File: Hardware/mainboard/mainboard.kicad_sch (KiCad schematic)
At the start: 31 parts, among them J1 Conn_01x06_Socket, J2 559592430, J3 USB_C_Receptacle_PowerOnly_24P, J5 SBH11-PBPC-D05-ST-BK, SW1 SW_SPDT, SW2 Board reset, SW3 Big reset, U1 S16B-PHDSSLFSN, U2 AMS1117-3.3, U3 STM32F091RCTx, Y1 16MHz

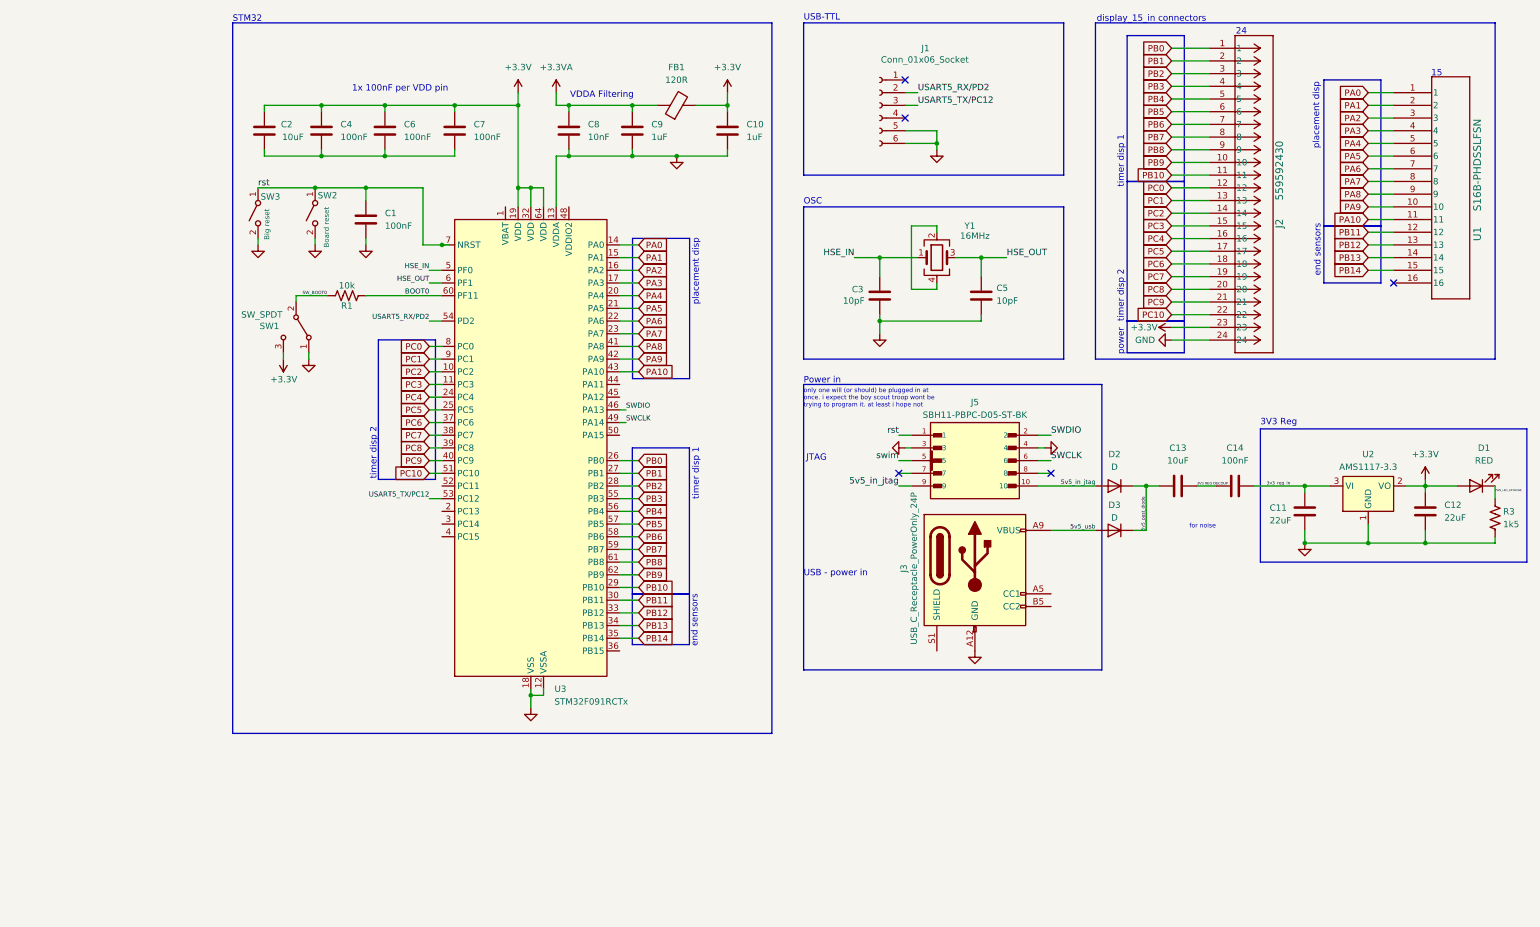
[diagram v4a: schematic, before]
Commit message: updated schematic
added:
-footprints
-status leds
-libraries
-connectors

separated into sheets since too many components on pange
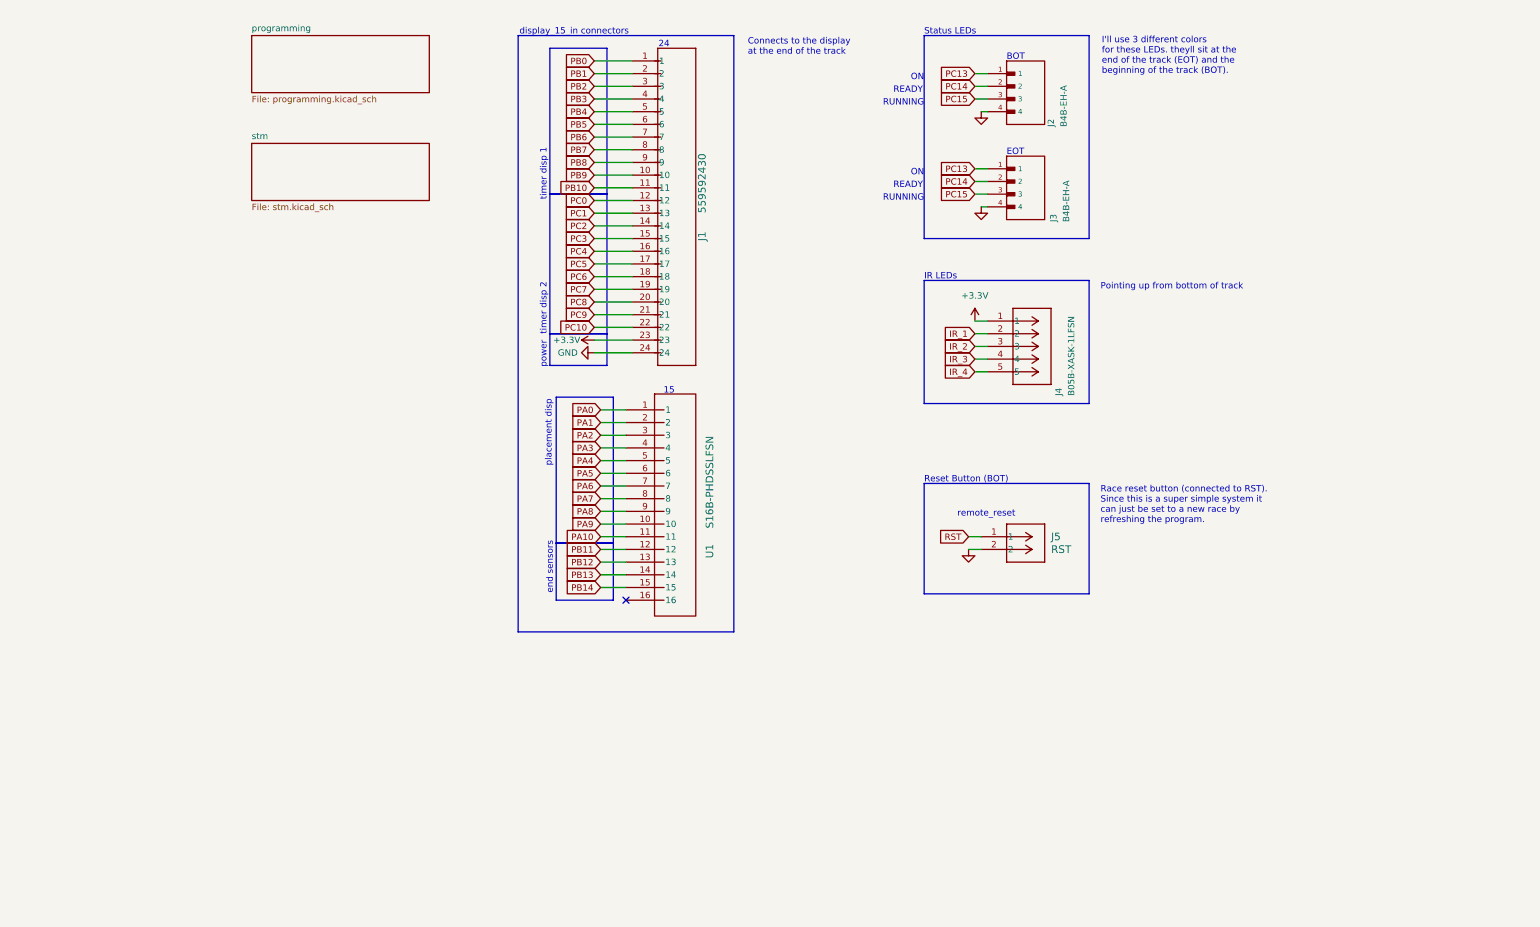
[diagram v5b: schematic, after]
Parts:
- removed C1, C14, C4, C6, C7: 100nF, Capacitor_SMD:C_0805_2012Metric, symbol Device:C
- removed C10, C9: 1uF, Capacitor_SMD:C_0805_2012Metric, symbol Device:C
- removed C11, C12: 22uF, Capacitor_SMD:C_0805_2012Metric, symbol Device:C
- removed C13, C2: 10uF, Capacitor_SMD:C_0805_2012Metric, symbol Device:C
- removed C3, C5: 10pF, Capacitor_SMD:C_0805_2012Metric, symbol Device:C
- removed C8: 10nF, Capacitor_SMD:C_0805_2012Metric, symbol Device:C
- removed D1: RED, Diode_SMD:D_0805_2012Metric, symbol Device:LED
- removed D2, D3: D, symbol Device:D
- removed FB1: 120R, Resistor_SMD:R_0805_2012Metric_Pad1.20x1.40mm_HandSolder, symbol Device:FerriteBead
- removed J1: Conn_01x06_Socket, jtag:SULLINS_SBH11-PBPC-D05-ST-BK, symbol Connector:Conn_01x06_Socket
- removed J3: USB_C_Receptacle_PowerOnly_24P, symbol Connector:USB_C_Receptacle_PowerOnly_24P
- removed J5: SBH11-PBPC-D05-ST-BK, SBH11-PBPC-D05-ST-BK:SULLINS_SBH11-PBPC-D05-ST-BK, symbol jtag:SBH11-PBPC-D05-ST-BK
- removed R1: 10k, Resistor_SMD:R_0805_2012Metric_Pad1.20x1.40mm_HandSolder, symbol Device:R_US
- removed R3: 1k5, Resistor_SMD:R_0805_2012Metric_Pad1.20x1.40mm_HandSolder, symbol Device:R_US
- removed SW1: SW_SPDT, symbol Switch:SW_SPDT
- removed SW2: Board reset, symbol Switch:SW_SPST
- removed SW3: Big reset, symbol Switch:SW_SPST
- removed U2: AMS1117-3.3, 3v3reg:SOT23-BEC, symbol Regulator_Linear:AMS1117-3.3
- removed U3: STM32F091RCTx, Package_QFP:LQFP-64_10x10mm_P0.5mm, symbol MCU_ST_STM32F0:STM32F091RCTx
- removed Y1: 16MHz, crystal smd:OSC_ECS-2520S25-250-FN-TR, symbol Device:Crystal_GND24
- added J2, J3: B4B-EH-A, 1x04_jst_connector:1x04_jst, symbol 1x04_jst:B4B-EH-A
- added J4: B05B-XASK-1LFSN, 1X05_JST:1x05_jst, symbol 1x05_jst:B05B-XASK-1LFSN
- added J5: RST, 1x02_jst_conn:CONN_B02B-XASK-1LFSN_JST, symbol 1x02_jst:B02B-XASK-1LFSN
- J1: renamed from J2; footprint 24pos 2mm:CONN24_559592430_MOL -> CONN24_559592430_MOL
- U1: footprint 16pos 2mm:S16B-PHDSSLFSN_JST -> S16B-PHDSSLFSN_JST
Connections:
- net +3.3V: now also J4.1
- net GND: now also J2.4, J3.4, J5.2
- new net IR_1: J4.2
- new net IR_2: J4.3
- new net IR_3: J4.4
- new net IR_4: J4.5
- new net PC13: J2.1, J3.1
- new net PC14: J2.2, J3.2
- new net PC15: J2.3, J3.3
- new net RST: J5.1
- no-connect marks 5 -> 1
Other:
- added sheet programming (programming.kicad_sch)
- added sheet stm (stm.kicad_sch)
- note added: "BOT"
- note added: "Connects to the display at the end of the track"
- note added: "EOT"
- note added: "I'll use 3 different colors for these LEDs. theyll sit at the end of the track (EOT) and the beginning of the track (BOT)."
- note added: "IR LEDs"
- note added: "ON"
- note added: "Pointing up from bottom of track"
- note added: "READY"
- note added: "RUNNING"
- note added: "Race reset button (connected to RST). Since this is a super simple system it can just be set to a new race by refreshing the program."
- note added: "Reset Button (BOT)"
- note added: "Status LEDs"
- note added: "remote_reset"
- note removed: "1x 100nF per VDD pin"
- note removed: "3V3 Reg"
- note removed: "JTAG"
- note removed: "OSC"
- note removed: "Power in"
- note removed: "STM32"
- note removed: "USB - power in"
- note removed: "USB-TTL"
- note removed: "VDDA Filtering"
- note removed: "for noise"
- note removed: "only one will (or should) be plugged in at once. i expect the boy scout troop wont be trying to program it. at least i hope not"

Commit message: pushing for the evening
didnt add much, just moved things around and fixed footprints
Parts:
- removed J5: RST, 1x02_jst_conn:CONN_B02B-XASK-1LFSN_JST, symbol 1x02_jst:B02B-XASK-1LFSN
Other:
- note removed: "Race reset button (connected to RST). Since this is a super simple system it can just be set to a new race by refreshing the program."
- note removed: "Reset Button (BOT)"
- note removed: "remote_reset"
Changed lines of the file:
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@@
 	(title_block
 		(title "F091RCT6 mainboard")
+		(date "2025-08-03")
 	)
 	(no_connect
@@
 	(wire
 		(pts
-			(xy 161.29 120.65) (xy 163.83 120.65)
-		)
-		(stroke
-			(width 0)
-			(type default)
-		)
-	)
-	(wire
-		(pts
 			(xy 92.71 95.25) (xy 87.63 95.25)
 		)
@@
 		(pts
 			(xy 86.36 50.8) (xy 93.98 50.8)
-		)
-		(stroke
-			(width 0)
-			(type default)
-		)
-	)
-	(wire
-		(pts
-			(xy 161.29 118.11) (xy 163.83 118.11)
 		)
 		(stroke
@@
 	)
 	(rectangle
-		(start 152.4 107.442)
-		(end 185.42 129.54)
-		(stroke
-			(width 0)
-			(type default)
-		)
-		(fill
-			(type none)
-		)
-	)
-	(rectangle
 		(start 77.47 49.53)
 		(end 88.9 77.47)
@@
 		)
 	)
-	(text "Reset Button (BOT)\n"
-		(exclude_from_sim no)
-		(at 152.4 106.68 0)
+	(text "BOT"
+		(exclude_from_sim no)
+		(at 168.91 22.098 0)
 		(effects
 			(font
@@
 		)
 	)
-	(text "remote_reset\n"
-		(exclude_from_sim no)
-		(at 164.846 113.538 0)
-		(effects
-			(font
-				(size 1.27 1.27)
-			)
-		)
-	)
-	(text "BOT"
-		(exclude_from_sim no)
-		(at 168.91 22.098 0)
+	(text "power\n"
+		(exclude_from_sim no)
+		(at 76.2 84.328 90)
 		(effects
 			(font
@@
 		)
 	)
-	(text "power\n"
-		(exclude_from_sim no)
-		(at 76.2 84.328 90)
+	(text "Connects to the display \nat the end of the track"
+		(exclude_from_sim no)
+		(at 117.094 18.288 0)
+		(effects
+			(font
+				(size 1.27 1.27)
+			)
+			(justify left top)
+		)
+	)
+	(text "I'll use 3 different colors\nfor these LEDs. theyll sit at the\nend of the track (EOT) and the\nbeginning of the track (BOT)."
+		(exclude_from_sim no)
+		(at 187.96 18.034 0)
+		(effects
+			(font
+				(size 1.27 1.27)
+			)
+			(justify left top)
+		)
+	)
+	(text "READY"
+		(exclude_from_sim no)
+		(at 152.146 28.702 0)
+		(effects
+			(font
+				(size 1.27 1.27)
+			)
+			(justify right)
+		)
+	)
+	(text "READY"
+		(exclude_from_sim no)
+		(at 152.146 47.752 0)
+		(effects
+			(font
+				(size 1.27 1.27)
+			)
+			(justify right)
+		)
+	)
+	(text "24\n"
+		(exclude_from_sim no)
+		(at 100.33 19.558 0)
+		(effects
+			(font
+				(size 1.27 1.27)
+			)
+		)
+	)
+	(text "15"
+		(exclude_from_sim no)
+		(at 101.346 88.9 0)
+		(effects
+			(font
+				(size 1.27 1.27)
+			)
+		)
+	)
+	(text "RUNNING\n"
+		(exclude_from_sim no)
+		(at 152.4 50.292 0)
+		(effects
+			(font
+				(size 1.27 1.27)
+			)
+			(justify right)
+		)
+	)
+	(text "timer disp 2\n\n"
+		(exclude_from_sim no)
+		(at 77.216 77.724 90)
 		(effects
 			(font
@@
 		)
 	)
-	(text "Connects to the display \nat the end of the track"
-		(exclude_from_sim no)
-		(at 117.094 18.288 0)
-		(effects
-			(font
-				(size 1.27 1.27)
-			)
-			(justify left top)
-		)
-	)
-	(text "I'll use 3 different colors\nfor these LEDs. theyll sit at the\nend of the track (EOT) and the\nbeginning of the track (BOT)."
-		(exclude_from_sim no)
-		(at 187.96 18.034 0)
-		(effects
-			(font
-				(size 1.27 1.27)
-			)
-			(justify left top)
-		)
-	)
-	(text "READY"
-		(exclude_from_sim no)
-		(at 152.146 28.702 0)
-		(effects
-			(font
-				(size 1.27 1.27)
-			)
-			(justify right)
-		)
-	)
-	(text "READY"
-		(exclude_from_sim no)
-		(at 152.146 47.752 0)
-		(effects
-			(font
-				(size 1.27 1.27)
-			)
-			(justify right)
-		)
-	)
-	(text "24\n"
-		(exclude_from_sim no)
-		(at 100.33 19.558 0)
-		(effects
-			(font
-				(size 1.27 1.27)
-			)
-		)
-	)
-	(text "15"
-		(exclude_from_sim no)
-		(at 101.346 88.9 0)
-		(effects
-			(font
-				(size 1.27 1.27)
-			)
-		)
-	)
-	(text "RUNNING\n"
-		(exclude_from_sim no)
-		(at 152.4 50.292 0)
-		(effects
-			(font
-				(size 1.27 1.27)
-			)
-			(justify right)
-		)
-	)
-	(text "Race reset button (connected to RST).\nSince this is a super simple system it\ncan just be set to a new race by \nrefreshing the program."
-		(exclude_from_sim no)
-		(at 187.706 107.95 0)
-		(effects
-			(font
-				(size 1.27 1.27)
-			)
-			(justify left top)
-		)
-	)
-	(text "timer disp 2\n\n"
-		(exclude_from_sim no)
-		(at 77.216 77.724 90)
+	(text "timer disp 1\n"
+		(exclude_from_sim no)
+		(at 76.2 50.8 90)
 		(effects
 			(font
@@
 		)
 	)
-	(text "timer disp 1\n"
-		(exclude_from_sim no)
-		(at 76.2 50.8 90)
-		(effects
-			(font
-				(size 1.27 1.27)
-			)
-			(justify left)
-		)
-	)
 	(global_label "PB4"
 		(shape input)
@@
 		(property "Intersheetrefs" "${INTERSHEET_REFS}"
 			(at 154.6158 49.53 0)
-			(effects
-				(font
-					(size 1.27 1.27)
-				)
-				(justify right)
-				(hide yes)
-			)
-		)
-	)
-	(global_label "RST"
-		(shape input)
-		(at 161.29 118.11 180)
-		(fields_autoplaced yes)
-		(effects
-			(font
-				(size 1.27 1.27)
-			)
-			(justify right)
-		)
-		(property "Intersheetrefs" "${INTERSHEET_REFS}"
-			(at 154.8577 118.11 0)
 			(effects
 				(font
@@
 	)
 	(symbol
-		(lib_id "power:GND")
-		(at 161.29 120.65 0)
-		(mirror y)
-		(unit 1)
-		(exclude_from_sim no)
-		(in_bom yes)
-		(on_board yes)
-		(dnp no)
-		(property "Reference" "#PWR06"
-			(at 161.29 127 0)
-			(effects
-				(font
-					(size 1.27 1.27)
-				)
-				(hide yes)
-			)
-		)
-		(property "Value" "GND"
-			(at 161.29 125.73 0)
-			(effects
-				(font
-					(size 1.27 1.27)
-				)
-				(hide yes)
-			)
-		)
-		(property "Footprint" ""
-			(at 161.29 120.65 0)
-			(effects
-				(font
-					(size 1.27 1.27)
-				)
-				(hide yes)
-			)
-		)
-		(property "Datasheet" ""
-			(at 161.29 120.65 0)
-			(effects
-				(font
-					(size 1.27 1.27)
-				)
-				(hide yes)
-			)
-		)
-		(property "Description" "Power symbol creates a global label with name \"GND\" , ground"
-			(at 161.29 120.65 0)
-			(effects
-				(font
-					(size 1.27 1.27)
-				)
-				(hide yes)
-			)
-		)
-		(pin "1"
-		)
-		(instances
-			(project "mainboard"
-				(path "/5f7c2eda-1e0f-4231-89f6-49a17b370d9e"
-					(reference "#PWR06")
-					(unit 1)
-				)
-			)
-		)
-	)
-	(symbol
 		(lib_id "power:+3.3V")
 		(at 162.56 74.93 0)
@@
 					(unit 1)
 				)
-			)
-		)
-	)
-	(symbol
-		(lib_id "1x02_jst:B02B-XASK-1LFSN")
-		(at 163.83 118.11 0)
-		(unit 1)
-		(exclude_from_sim no)
-		(in_bom yes)
-		(on_board yes)
-		(dnp no)
-		(property "Reference" "J5"
-			(at 177.8 118.1099 0)
-			(effects
-				(font
-					(size 1.524 1.524)
-				)
-				(justify left)
-			)
-		)
-		(property "Value" "RST"
-			(at 177.8 120.6499 0)
-			(effects
-				(font
-					(size 1.524 1.524)
-				)
-				(justify left)
-			)
-		)
-		(property "Footprint" "1x02_jst_conn:CONN_B02B-XASK-1LFSN_JST"
-			(at 163.83 118.11 0)
-			(effects
-				(font
-					(size 1.27 1.27)
-					(italic yes)
-				)
-				(hide yes)
-			)
-		)
-		(property "Datasheet" "B02B-XASK-1LFSN"
-			(at 163.83 118.11 0)
-			(effects
-				(font
-					(size 1.27 1.27)
-					(italic yes)
-				)
-				(hide yes)
-			)
-		)
-		(property "Description" ""
-			(at 163.83 118.11 0)
-			(effects
-				(font
-					(size 1.27 1.27)
-				)
-				(hide yes)
-			)
-		)
-		(pin "2"
-		)
-		(pin "1"
-		)
-		(instances
-			(project ""
-				(path "/5f7c2eda-1e0f-4231-89f6-49a17b370d9e"
-					(reference "J5")
-					(unit 1)
-				)

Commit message: add layer
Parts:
- J2: value B4B-EH-A -> status bot
- J3: value B4B-EH-A -> status eot
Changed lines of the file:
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@@
 			)
 		)
-		(property "Value" "B4B-EH-A"
+		(property "Value" "status bot"
 			(at 180.34 36.068 90)
 			(effects
@@
 			)
 		)
-		(property "Value" "B4B-EH-A"
+		(property "Value" "status eot"
 			(at 180.848 55.118 90)
 			(effects

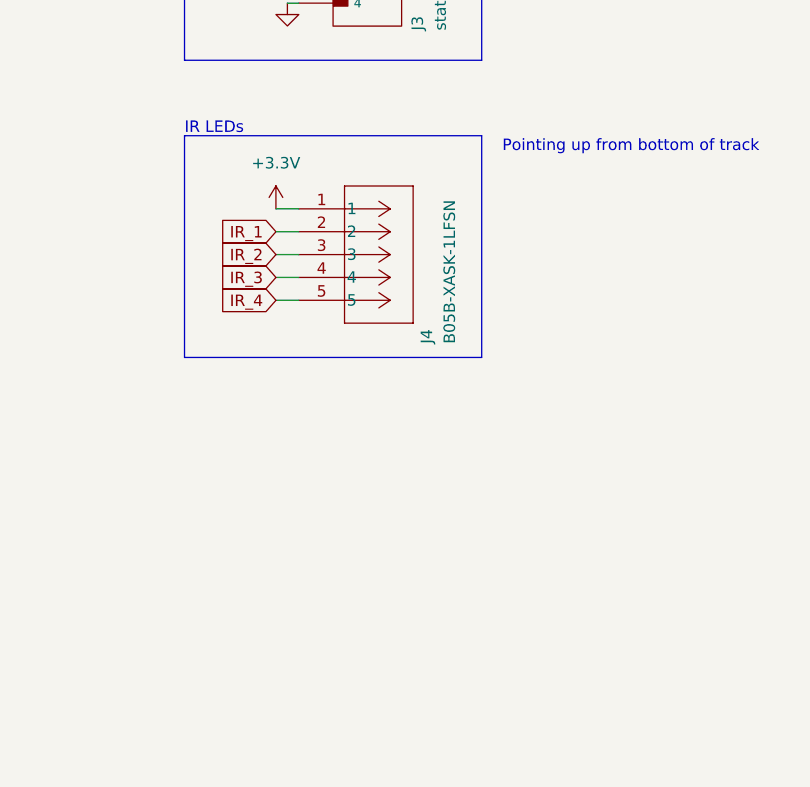
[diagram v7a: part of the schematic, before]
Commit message: fixed schematic pcb agreement errors
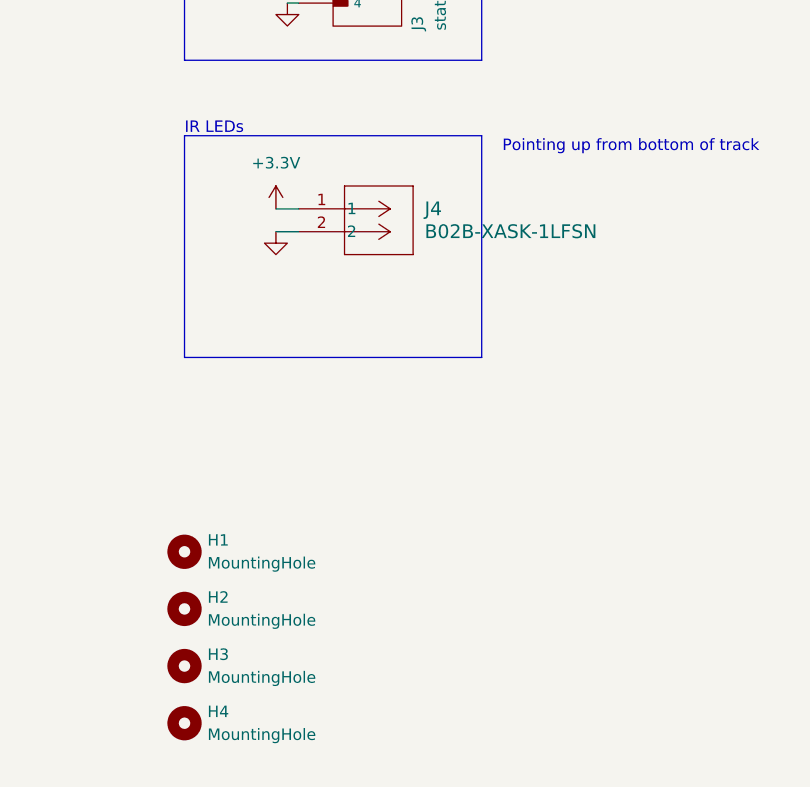
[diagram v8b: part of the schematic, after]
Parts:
- removed J4: B05B-XASK-1LFSN, 1X05_JST:1x05_jst, symbol 1x05_jst:B05B-XASK-1LFSN
- added H1, H2, H3, H4: MountingHole, MountingHole:MountingHole_4.3mm_M4_DIN965, symbol Mechanical:MountingHole
- added J4: B02B-XASK-1LFSN, BIG LIBRARY:1X02_JST, symbol 1x02_jst:B02B-XASK-1LFSN
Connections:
- net +3.3V: now also J4.1
- net GND: now also J4.2
